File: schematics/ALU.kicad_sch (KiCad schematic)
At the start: 22 parts, among them U1 74LS283, U2 74LS283, U3 74LS245, U4 74LS86, U5 74LS86

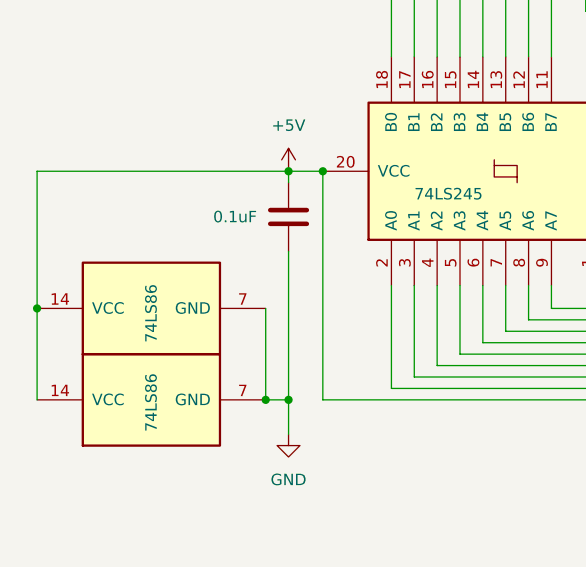
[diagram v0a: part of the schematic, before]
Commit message: feat: updated electrical diagrams & individual part list
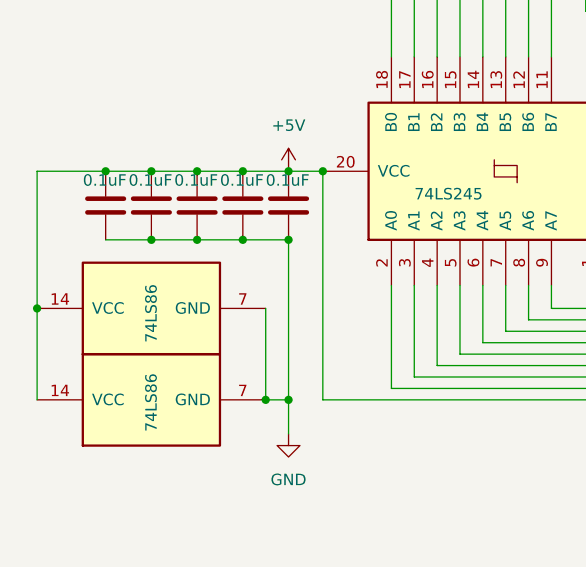
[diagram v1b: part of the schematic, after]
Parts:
- added C2, C3, C4, C5: 0.1uF, symbol Device:C
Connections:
- net +5V: now also C2.1, C3.1, C4.1, C5.1
- net GND: now also C2.2, C3.2, C4.2, C5.2
